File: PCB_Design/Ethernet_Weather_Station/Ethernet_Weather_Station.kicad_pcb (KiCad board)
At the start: 2 copper layers, 177 parts, among them J1 USB_C_Receptacle_USB2.0_16P, J10 RJ45_LED_Shielded, J11 PD0~7, J2 Conn_02x06, J3 RS485, J4 Conn_02x04, J5 Conn_02x04, J6 PE_PF, J7 JTAG, J8 PC, J9 PB0~7, Q1 BSN20, Q2 BSN20, Q3 BSN20, Q4 BSN20, Q5 BSN20, Q6 BSN20, Q7 2N7002, SW1 Button, SW2 SW_SPDT, U1 ADS1220xPW, U10 LM76002, U11 TPS2375-1, U2 ATmega32U4-M, U3 ADS1220xPW, U4 AW9523B, U5 ADM2483xRW, U6 W5500, U7 DS1302Z+, U8 SHT4x, U9 LM76002, Y1 16MHz, Y2 Crystal, Y3 32.768kHz

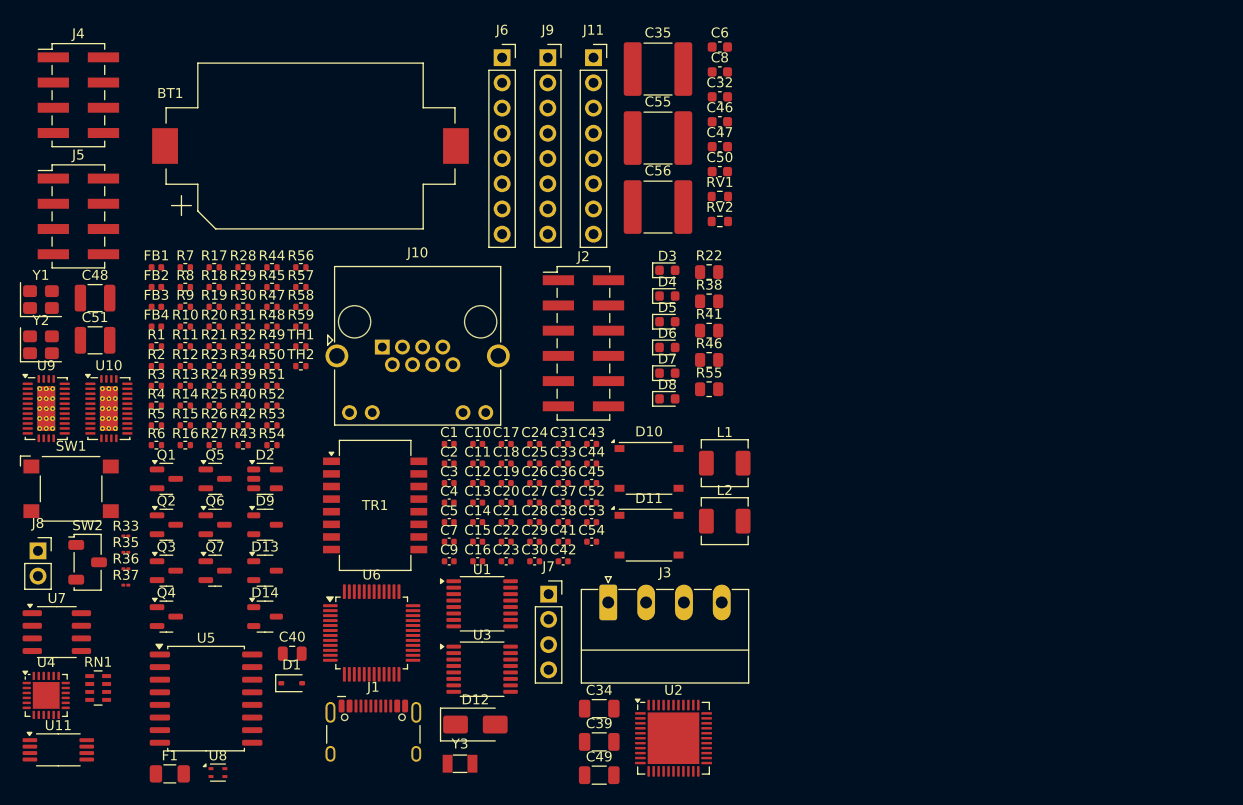
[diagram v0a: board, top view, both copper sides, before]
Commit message: " add EDC protecion"
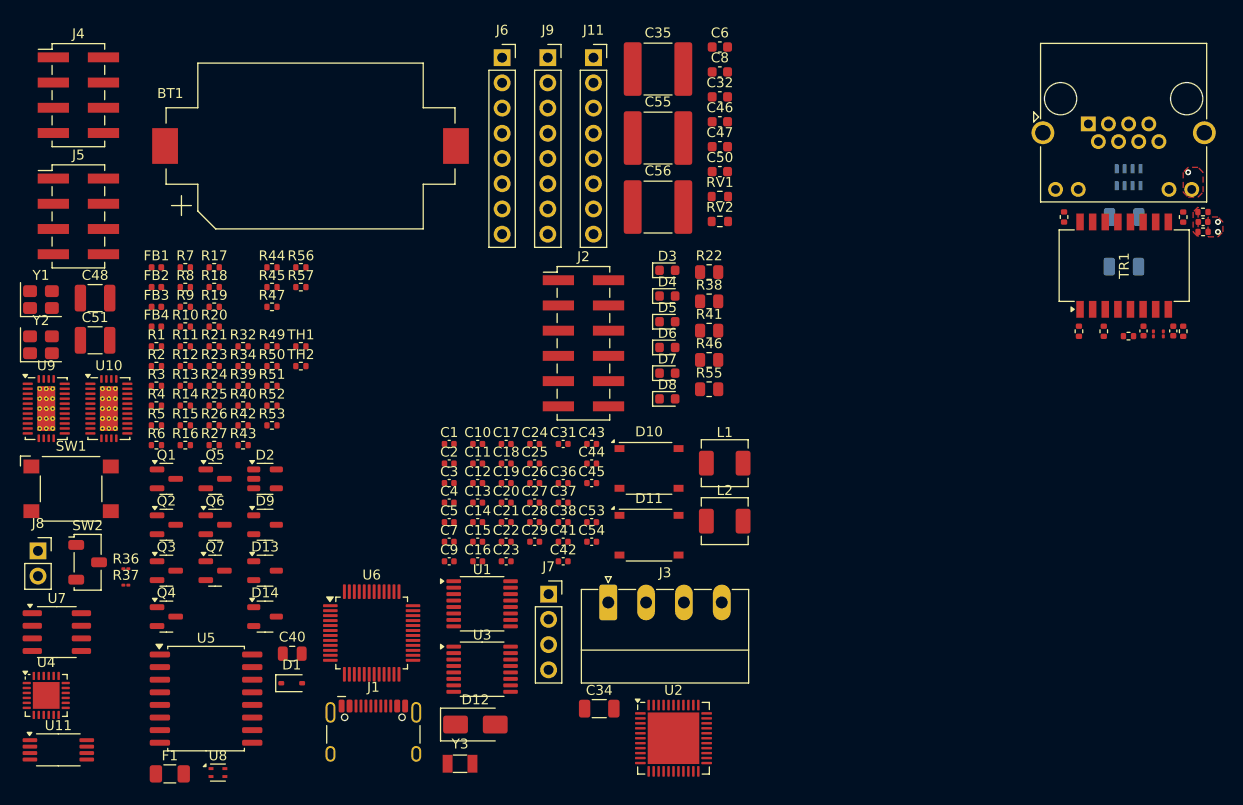
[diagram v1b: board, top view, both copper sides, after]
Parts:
- C39, C49, RN1: moved to B.Cu
- moved RN1 115.8 mm to (204.0, 45.5), turned to -90 degrees
- moved R35 106.8 mm to (207.5, 61.3), turned to 90 degrees
- moved R33 105.5 mm to (206.5, 61.3), turned to 90 degrees
- moved R54 96.7 mm to (211.5, 49.0), turned to 180 degrees
- moved R30 94.7 mm to (209.5, 61.0), turned to -90 degrees
- moved R48 94.3 mm to (211.5, 51.0)
- moved R58 89.3 mm to (209.5, 49.5), turned to -90 degrees
- moved R31 89.2 mm to (204.0, 61.5)
- moved R28 86.9 mm to (201.5, 61.0), turned to 90 degrees
- moved R29 84.3 mm to (199.0, 61.0), turned to 90 degrees
- moved TR1 79.2 mm to (203.6, 54.4), turned to 90 degrees
- moved R59 77.7 mm to (197.5, 49.5), turned to -90 degrees
- moved C39 74.8 mm to (203.6, 49.5)
- moved J10 74.6 mm to (199.9, 40.1)
- moved C49 73.6 mm to (203.5, 54.5), turned to 180 degrees
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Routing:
- net (no net): vias 0 -> 3
- added copper zone on F.Cu, net +3.3V
- added copper zone on F.Cu, net GND
- added copper zone on F.Cu, net Net-(C52-Pad1)
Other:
- copper layers 2 -> 4
